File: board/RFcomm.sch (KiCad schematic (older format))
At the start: 17 parts, among them U3 nrf24l01, Y3 16 MHz

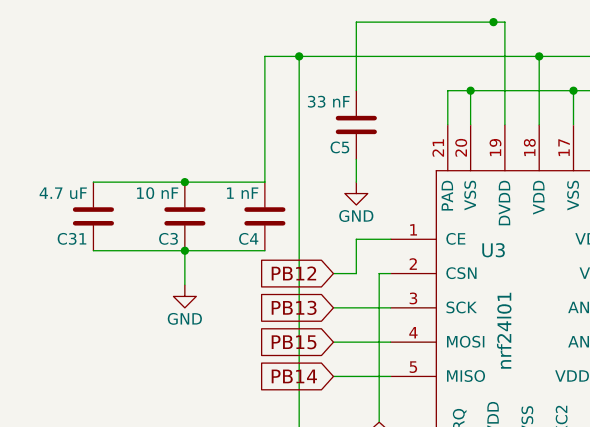
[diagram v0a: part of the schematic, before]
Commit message: Moved around components and added cutouts
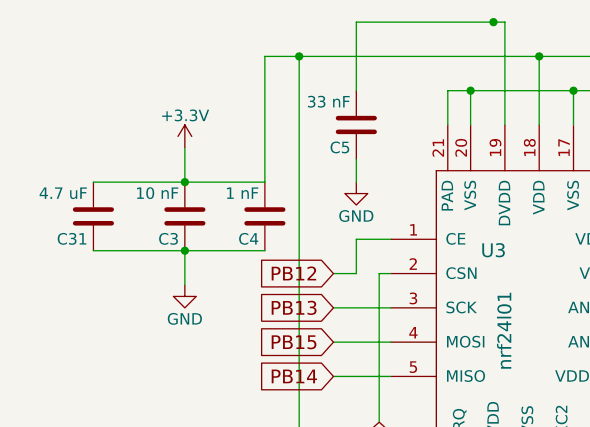
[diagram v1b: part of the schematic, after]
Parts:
- C18: LCSC C1546 -> C1550
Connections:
- net labels added: +3.3V
- wire segments 56 -> 57
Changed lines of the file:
@@
 $Descr A4 11693 8268
 encoding utf-8
-Sheet 3 9
+Sheet 3 10
 Title ""
 Date ""
@@
 $EndComp
 $Comp
-L GND #PWR44
+L GND #PWR48
 U 1 1 5EA4CDA1
 P 6400 2850
-F 0 "#PWR44" H 6400 2600 50  0001 C CNN
+F 0 "#PWR48" H 6400 2600 50  0001 C CNN
 F 1 "GND" H 6400 2700 50  0000 C CNN
 F 2 "" H 6400 2850 50  0001 C CNN
@@
 $EndComp
 $Comp
-L GND #PWR46
+L GND #PWR50
 U 1 1 5EA4D30A
 P 7900 4000
-F 0 "#PWR46" H 7900 3750 50  0001 C CNN
+F 0 "#PWR50" H 7900 3750 50  0001 C CNN
 F 1 "GND" H 7900 3850 50  0000 C CNN
 F 2 "" H 7900 4000 50  0001 C CNN
@@
 $EndComp
 $Comp
-L GND #PWR50
+L GND #PWR54
 U 1 1 5EA4D41A
 P 8750 2800
-F 0 "#PWR50" H 8750 2550 50  0001 C CNN
+F 0 "#PWR54" H 8750 2550 50  0001 C CNN
 F 1 "GND" H 8900 2800 50  0000 C CNN
 F 2 "" H 8750 2800 50  0001 C CNN
@@
 $EndComp
 $Comp
-L GND #PWR49
+L GND #PWR53
 U 1 1 5EA4D52B
 P 8600 2200
-F 0 "#PWR49" H 8600 1950 50  0001 C CNN
+F 0 "#PWR53" H 8600 1950 50  0001 C CNN
 F 1 "GND" H 8600 2050 50  0000 C CNN
 F 2 "" H 8600 2200 50  0001 C CNN
@@
 $EndComp
 $Comp
-L GND #PWR47
+L GND #PWR51
 U 1 1 5EA4E0F6
 P 8000 5250
-F 0 "#PWR47" H 8000 5000 50  0001 C CNN
+F 0 "#PWR51" H 8000 5000 50  0001 C CNN
 F 1 "GND" H 8000 5100 50  0000 C CNN
 F 2 "" H 8000 5250 50  0001 C CNN
@@
 $EndComp
 $Comp
-L GND #PWR48
+L GND #PWR52
 U 1 1 5EA4E551
 P 8300 5250
-F 0 "#PWR48" H 8300 5000 50  0001 C CNN
+F 0 "#PWR52" H 8300 5000 50  0001 C CNN
 F 1 "GND" H 8300 5100 50  0000 C CNN
 F 2 "" H 8300 5250 50  0001 C CNN
@@
 $EndComp
 $Comp
-L GND #PWR51
+L GND #PWR55
 U 1 1 5EA4F3B2
 P 8900 4050
-F 0 "#PWR51" H 8900 3800 50  0001 C CNN
+F 0 "#PWR55" H 8900 3800 50  0001 C CNN
 F 1 "GND" H 8900 3900 50  0000 C CNN
 F 2 "" H 8900 4050 50  0001 C CNN
@@
 $EndComp
 $Comp
-L GND #PWR53
+L GND #PWR57
 U 1 1 5EA4F86C
 P 9300 4050
-F 0 "#PWR53" H 9300 3800 50  0001 C CNN
+F 0 "#PWR57" H 9300 3800 50  0001 C CNN
 F 1 "GND" H 9300 3900 50  0000 C CNN
 F 2 "" H 9300 4050 50  0001 C CNN
@@
 F 2 "Capacitors_SMD:C_0402_NoSilk" H 9888 2950 50  0001 C CNN
 F 3 "" H 9850 3100 50  0001 C CNN
-F 4 "C1546" H 9850 3100 60  0001 C CNN "LCSC"
+F 4 "C1550" H 9850 3100 60  0001 C CNN "LCSC"
 	1    9850 3100
 	-1   0    0    1
@@
 $EndComp
 $Comp
-L GND #PWR54
+L GND #PWR58
 U 1 1 5EA4FF18
 P 9850 3300
-F 0 "#PWR54" H 9850 3050 50  0001 C CNN
+F 0 "#PWR58" H 9850 3050 50  0001 C CNN
 F 1 "GND" H 9850 3150 50  0000 C CNN
 F 2 "" H 9850 3300 50  0001 C CNN
@@
 $EndComp
 $Comp
-L GND #PWR52
+L GND #PWR56
 U 1 1 5EA506C6
 P 9250 2200
-F 0 "#PWR52" H 9250 1950 50  0001 C CNN
+F 0 "#PWR56" H 9250 1950 50  0001 C CNN
 F 1 "GND" H 9250 2050 50  0000 C CNN
 F 2 "" H 9250 2200 50  0001 C CNN
@@
 $EndComp
 $Comp
-L GND #PWR45
+L GND #PWR49
 U 1 1 5EA50B2C
 P 7150 2400
-F 0 "#PWR45" H 7150 2150 50  0001 C CNN
+F 0 "#PWR49" H 7150 2150 50  0001 C CNN
 F 1 "GND" H 7150 2250 50  0000 C CNN
 F 2 "" H 7150 2400 50  0001 C CNN
@@
 F 2 "Capacitors_SMD:C_0805" H 6038 2400 50  0001 C CNN
 F 3 "" H 6000 2550 50  0001 C CNN
-F 4 "C15195" H 6000 2550 60  0001 C CNN "LCSC"
-F 5 "C1779" H 6000 2550 60  0001 C CNN "LCSC"
+F 4 "C1779" H 6000 2550 60  0001 C CNN "LCSC"
 	1    6000 2550
 	-1   0    0    1
@@
 Connection ~ 6400 2400
 Connection ~ 6400 2700
+$Comp
+L +3.3V #PWR47
+U 1 1 5EB434E0
+P 6400 2250
+F 0 "#PWR47" H 6400 2100 50  0001 C CNN
+F 1 "+3.3V" H 6400 2390 50  0000 C CNN
+F 2 "" H 6400 2250 50  0001 C CNN
+F 3 "" H 6400 2250 50  0001 C CNN
+	1    6400 2250
+	1    0    0    -1
+$EndComp
+Wire Wire Line
+	6400 2250 6400 2400
 $EndSCHEMATC

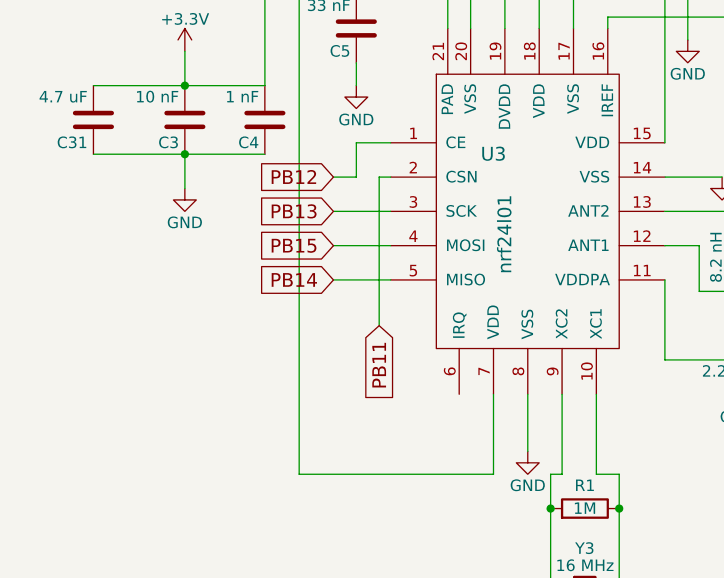
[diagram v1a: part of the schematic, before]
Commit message: Moved the brushes to the other side of the board
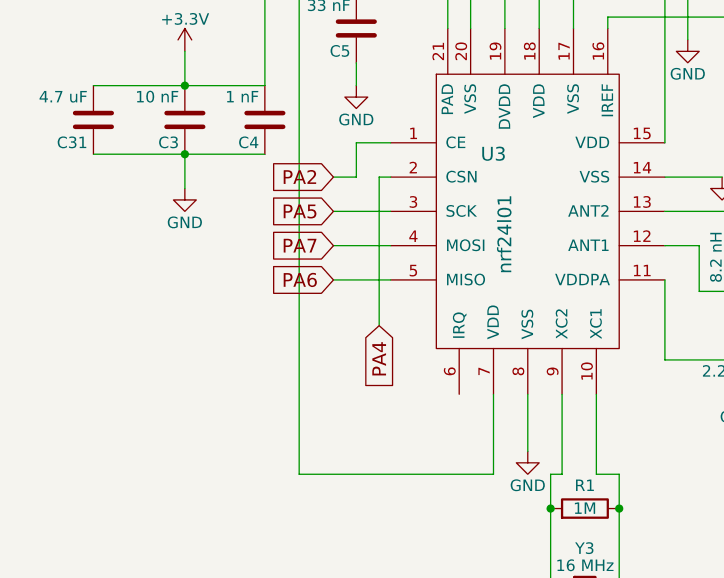
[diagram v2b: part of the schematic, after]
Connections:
- net labels added: PA2, PA4, PA5, PA6, PA7
- net labels removed: PB11, PB12, PB13, PB14, PB15
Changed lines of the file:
@@
 $EndComp
 Text GLabel 7050 2950 0    60   Input ~ 0
-PB13
+PA5
 Text GLabel 7050 3250 0    60   Input ~ 0
-PB14
+PA6
 Text GLabel 7050 3100 0    60   Input ~ 0
-PB15
+PA7
 Text GLabel 7050 2800 0    60   Input ~ 0
-PB12
+PA2
 Text GLabel 7250 3450 3    60   Input ~ 0
-PB11
+PA4
 Wire Wire Line
 	6400 2850 6400 2700
